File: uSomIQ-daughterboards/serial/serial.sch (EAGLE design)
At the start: 76 parts, among them IC401 DS3231/SO, P101 189-009-613R571, P102 83611-9006, P103 189-009-613R571, P301 USOMIQ-AM335X, U201 TPS54260, U401 ADM3311E, U402 ADM3311E, X301 MINI-USB-UX60-MB-5ST

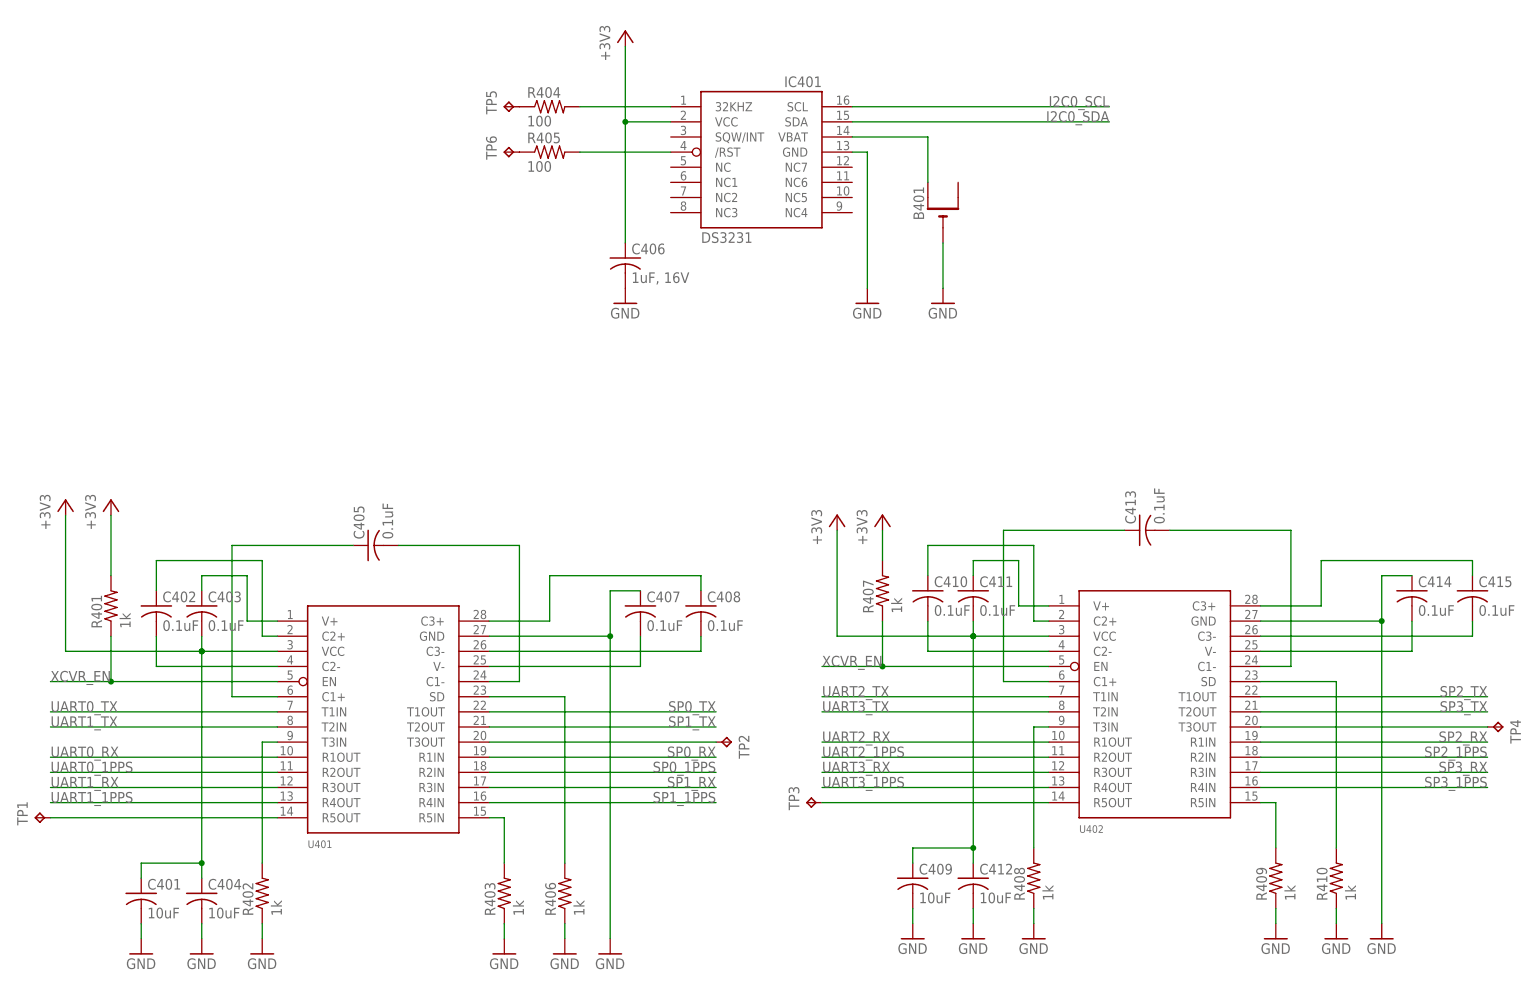
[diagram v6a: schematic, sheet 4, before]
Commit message: Initial part placement for serial daughterboard
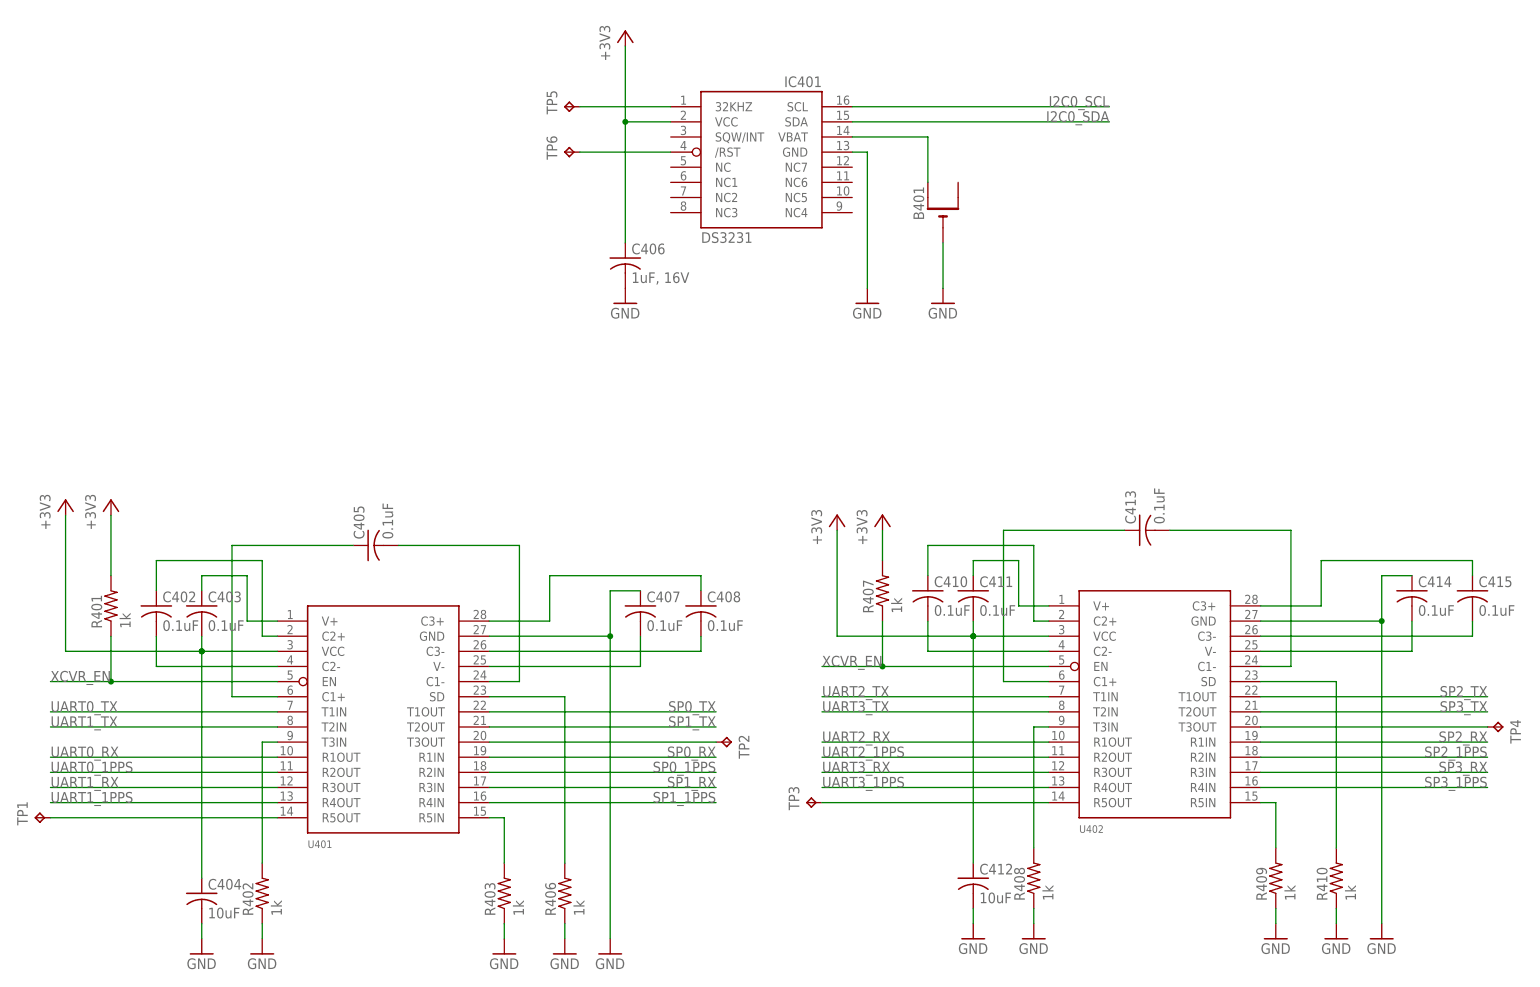
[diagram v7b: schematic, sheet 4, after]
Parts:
- removed C401, C409: 10uF, resistor:C-USC0603
- removed R404, R405: 100, rcl:R-US_R0603
- D208, D209: device diode:ZENER-DIODESMB -> diode:ZENER-DIODESOT23
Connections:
- removed net N$1: R404.1, TP5.TP
- removed net N$41: R405.1, TP6.TP
- net +3V3: no longer C401.1, C409.1
- net GND: no longer C401.2, C409.2
- net N$39: now also TP6.TP; no longer R405.2
- net N$8: now also TP5.TP; no longer R404.2
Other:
- moved on the sheet: TP5, TP6
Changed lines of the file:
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@@
 <part name="TB401" library="titleblock" deviceset="REDLINE-TITLEBLOCK" device=""/>
 <part name="IC401" library="adafruit" deviceset="DS3231" device="/SO"/>
-<part name="R404" library="rcl" deviceset="R-US_" device="R0603" value="100"/>
 <part name="C406" library="rcl" deviceset="C-US" device="C0603" value="1uF, 16V"/>
 <part name="GND407" library="supply1" deviceset="GND" device=""/>
@@
 <part name="GND406" library="supply1" deviceset="GND" device=""/>
 <part name="+3V3401" library="supply1" deviceset="+3V3" device=""/>
-<part name="C401" library="resistor" deviceset="C-US" device="C0603" value="10uF"/>
 <part name="C404" library="resistor" deviceset="C-US" device="C0603" value="10uF"/>
 <part name="GND402" library="supply1" deviceset="GND" device=""/>
-<part name="GND401" library="supply1" deviceset="GND" device=""/>
 <part name="U402" library="misc-ics" deviceset="ADM3311E" device=""/>
 <part name="C411" library="resistor" deviceset="C-US" device="C0603" value="0.1uF"/>
@@
 <part name="GND415" library="supply1" deviceset="GND" device=""/>
 <part name="+3V3404" library="supply1" deviceset="+3V3" device=""/>
-<part name="C409" library="resistor" deviceset="C-US" device="C0603" value="10uF"/>
 <part name="C412" library="resistor" deviceset="C-US" device="C0603" value="10uF"/>
 <part name="GND411" library="supply1" deviceset="GND" device=""/>
-<part name="GND409" library="supply1" deviceset="GND" device=""/>
 <part name="R401" library="resistor" deviceset="R-US_" device="R0603" value="1k"/>
 <part name="R407" library="resistor" deviceset="R-US_" device="R0603" value="1k"/>
@@
 <part name="D202" library="diode" deviceset="BAS40" device=""/>
 <part name="+3V3403" library="supply1" deviceset="+3V3" device=""/>
-<part name="R405" library="rcl" deviceset="R-US_" device="R0603" value="100"/>
 <part name="R209" library="rcl" deviceset="R-US_" device="R0603" value="20K"/>
 <part name="C210" library="rcl" deviceset="C-US" device="C0603" value="0.1uF"/>
@@
 <part name="GND203" library="supply1" deviceset="GND" device=""/>
 <part name="D207" library="diode" deviceset="BAS40" device=""/>
-<part name="D208" library="diode" deviceset="ZENER-DIODE" device="SMB" value="1.8V"/>
+<part name="D208" library="diode" deviceset="ZENER-DIODE" device="SOT23" value="1.8V"/>
 <part name="GND215" library="supply1" deviceset="GND" device=""/>
 <part name="R210" library="rcl" deviceset="R-US_" device="R0603" value="20K"/>
-<part name="D209" library="diode" deviceset="ZENER-DIODE" device="SMB" value="1.8V"/>
+<part name="D209" library="diode" deviceset="ZENER-DIODE" device="SOT23" value="1.8V"/>
 <part name="R212" library="rcl" deviceset="R-US_" device="R0603" value="1K"/>
 <part name="C211" library="rcl" deviceset="C-US" device="C0603" value="0.1uF"/>
@@
 <instance part="TB401" gate="G$1" x="0" y="0"/>
 <instance part="IC401" gate="G$1" x="137.16" y="170.18"/>
-<instance part="R404" gate="G$1" x="101.6" y="180.34"/>
 <instance part="C406" gate="G$1" x="114.3" y="154.94"/>
 <instance part="GND407" gate="1" x="114.3" y="147.32"/>
@@
 <instance part="GND406" gate="1" x="111.76" y="38.1"/>
 <instance part="+3V3401" gate="G$1" x="20.32" y="114.3"/>
-<instance part="C401" gate="G$1" x="33.02" y="48.26"/>
 <instance part="C404" gate="G$1" x="43.18" y="48.26"/>
 <instance part="GND402" gate="1" x="43.18" y="38.1"/>
-<instance part="GND401" gate="1" x="33.02" y="38.1"/>
 <instance part="U402" gate="G$1" x="190.5" y="66.04"/>
 <instance part="C411" gate="G$1" x="172.72" y="99.06"/>
@@
 <instance part="GND415" gate="1" x="241.3" y="40.64"/>
 <instance part="+3V3404" gate="G$1" x="149.86" y="111.76"/>
-<instance part="C409" gate="G$1" x="162.56" y="50.8"/>
 <instance part="C412" gate="G$1" x="172.72" y="50.8"/>
 <instance part="GND411" gate="1" x="172.72" y="40.64"/>
-<instance part="GND409" gate="1" x="162.56" y="40.64"/>
 <instance part="R401" gate="G$1" x="27.94" y="96.52" rot="R90"/>
 <instance part="R407" gate="G$1" x="157.48" y="99.06" rot="R90"/>
@@
 <instance part="+3V3405" gate="G$1" x="157.48" y="111.76"/>
 <instance part="+3V3403" gate="G$1" x="114.3" y="193.04"/>
-<instance part="R405" gate="G$1" x="101.6" y="172.72"/>
-<instance part="TP5" gate="G$1" x="93.98" y="180.34" rot="R90"/>
-<instance part="TP6" gate="G$1" x="93.98" y="172.72" rot="R90"/>
+<instance part="TP5" gate="G$1" x="104.14" y="180.34" rot="R90"/>
+<instance part="TP6" gate="G$1" x="104.14" y="172.72" rot="R90"/>
 </instances>
 <busses>
@@
 </segment>
 <segment>
-<pinref part="C401" gate="G$1" pin="2"/>
-<pinref part="GND401" gate="1" pin="GND"/>
-<wire x1="33.02" y1="43.18" x2="33.02" y2="40.64" width="0.1524" layer="91"/>
-</segment>
-<segment>
 <pinref part="C404" gate="G$1" pin="2"/>
 <pinref part="GND402" gate="1" pin="GND"/>
@@
 </segment>
 <segment>
-<pinref part="C409" gate="G$1" pin="2"/>
-<pinref part="GND409" gate="1" pin="GND"/>
-<wire x1="162.56" y1="45.72" x2="162.56" y2="43.18" width="0.1524" layer="91"/>
-</segment>
-<segment>
 <pinref part="C412" gate="G$1" pin="2"/>
 <pinref part="GND411" gate="1" pin="GND"/>
@@
 <segment>
 <pinref part="IC401" gate="G$1" pin="32KHZ"/>
-<pinref part="R404" gate="G$1" pin="2"/>
 <wire x1="121.92" y1="180.34" x2="106.68" y2="180.34" width="0.1524" layer="91"/>
+<pinref part="TP5" gate="G$1" pin="TP"/>
 </segment>
 </net>
@@
 <junction x="43.18" y="88.9"/>
 <pinref part="C404" gate="G$1" pin="1"/>
-<wire x1="43.18" y1="50.8" x2="43.18" y2="53.34" width="0.1524" layer="91"/>
 <junction x="43.18" y="88.9"/>
-<pinref part="C401" gate="G$1" pin="1"/>
-<wire x1="43.18" y1="53.34" x2="43.18" y2="88.9" width="0.1524" layer="91"/>
-<wire x1="43.18" y1="53.34" x2="33.02" y2="53.34" width="0.1524" layer="91"/>
-<wire x1="33.02" y1="53.34" x2="33.02" y2="50.8" width="0.1524" layer="91"/>
-<junction x="43.18" y="53.34"/>
+<wire x1="43.18" y1="50.8" x2="43.18" y2="88.9" width="0.1524" layer="91"/>
 </segment>
 <segment>
@@
 <junction x="172.72" y="91.44"/>
 <pinref part="C412" gate="G$1" pin="1"/>
-<wire x1="172.72" y1="53.34" x2="172.72" y2="55.88" width="0.1524" layer="91"/>
 <junction x="172.72" y="91.44"/>
-<pinref part="C409" gate="G$1" pin="1"/>
-<wire x1="172.72" y1="55.88" x2="172.72" y2="91.44" width="0.1524" layer="91"/>
-<wire x1="172.72" y1="55.88" x2="162.56" y2="55.88" width="0.1524" layer="91"/>
-<wire x1="162.56" y1="55.88" x2="162.56" y2="53.34" width="0.1524" layer="91"/>
-<junction x="172.72" y="55.88"/>
+<wire x1="172.72" y1="53.34" x2="172.72" y2="91.44" width="0.1524" layer="91"/>
 </segment>
 <segment>
@@
 <segment>
 <pinref part="IC401" gate="G$1" pin="/RST"/>
-<pinref part="R405" gate="G$1" pin="2"/>
 <wire x1="121.92" y1="172.72" x2="106.68" y2="172.72" width="0.1524" layer="91"/>
-</segment>
-</net>
-<net name="N$1" class="0">
-<segment>
-<pinref part="R404" gate="G$1" pin="1"/>
-<pinref part="TP5" gate="G$1" pin="TP"/>
-</segment>
-</net>
-<net name="N$41" class="0">
-<segment>
-<pinref part="R405" gate="G$1" pin="1"/>
 <pinref part="TP6" gate="G$1" pin="TP"/>
 </segment>
